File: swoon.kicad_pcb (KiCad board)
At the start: 2 copper layers, 109 x 86.9 mm, 130 parts, among them J1 3305-0-15-80-47-27-10-0, J10 3305-0-15-80-47-27-10-0, J11 3305-0-15-80-47-27-10-0, J12 3305-0-15-80-47-27-10-0, J13 3305-0-15-80-47-27-10-0, J14 3305-0-15-80-47-27-10-0, J15 3305-0-15-80-47-27-10-0, J16 3305-0-15-80-47-27-10-0, J17 3305-0-15-80-47-27-10-0, J18 3305-0-15-80-47-27-10-0, J19 3305-0-15-80-47-27-10-0, J2 3305-0-15-80-47-27-10-0, J20 3305-0-15-80-47-27-10-0, J21 3305-0-15-80-47-27-10-0, J22 3305-0-15-80-47-27-10-0, J23 3305-0-15-80-47-27-10-0, J24 3305-0-15-80-47-27-10-0, J25 3305-0-15-80-47-27-10-0, J26 3305-0-15-80-47-27-10-0, J27 3305-0-15-80-47-27-10-0, J28 3305-0-15-80-47-27-10-0, J29 3305-0-15-80-47-27-10-0, J3 3305-0-15-80-47-27-10-0, J30 3305-0-15-80-47-27-10-0, J31 3305-0-15-80-47-27-10-0, J32 3305-0-15-80-47-27-10-0, J33 3305-0-15-80-47-27-10-0, J34 3305-0-15-80-47-27-10-0, J35 3305-0-15-80-47-27-10-0, J36 3305-0-15-80-47-27-10-0, J37 3305-0-15-80-47-27-10-0, J38 3305-0-15-80-47-27-10-0, J39 3305-0-15-80-47-27-10-0, J4 3305-0-15-80-47-27-10-0, J40 3305-0-15-80-47-27-10-0, J41 3305-0-15-80-47-27-10-0, J42 3305-0-15-80-47-27-10-0, J43 3305-0-15-80-47-27-10-0, J44 3305-0-15-80-47-27-10-0, J45 3305-0-15-80-47-27-10-0, J46 3305-0-15-80-47-27-10-0, J47 3305-0-15-80-47-27-10-0, J48 3305-0-15-80-47-27-10-0, J49 3305-0-15-80-47-27-10-0, J5 3305-0-15-80-47-27-10-0, J50 3305-0-15-80-47-27-10-0, J51 3305-0-15-80-47-27-10-0, J52 3305-0-15-80-47-27-10-0, J53 3305-0-15-80-47-27-10-0, J54 3305-0-15-80-47-27-10-0, J55 3305-0-15-80-47-27-10-0, J56 3305-0-15-80-47-27-10-0, J57 3305-0-15-80-47-27-10-0, J58 3305-0-15-80-47-27-10-0, J59 3305-0-15-80-47-27-10-0, J6 3305-0-15-80-47-27-10-0, J60 3305-0-15-80-47-27-10-0, J61 3305-0-15-80-47-27-10-0, J62 3305-0-15-80-47-27-10-0, J63 3305-0-15-80-47-27-10-0, J64 3305-0-15-80-47-27-10-0, J65 3305-0-15-80-47-27-10-0, J66 3305-0-15-80-47-27-10-0, J67 3305-0-15-80-47-27-10-0, J68 3305-0-15-80-47-27-10-0, J69 MF254V-11-07-0743, J7 3305-0-15-80-47-27-10-0, J70 MF254V-11-07-0743, J71 MF254V-11-07-0743, J72 MF254V-11-07-0743, J73 Mill Max 0906-2-15-20-75-14-1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, J74 Mill Max 0906-2-15-20-75-14-1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, J75 JST SM02B-SRSS-TB(LF)(SN), J76 JST SM02B-SRSS-TB(LF)(SN), J8 3305-0-15-80-47-27-10-0, J9 3305-0-15-80-47-27-10-0, SW1 SW_Push, SW10 SW_Push, SW11 SW_Push, SW12 SW_Push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

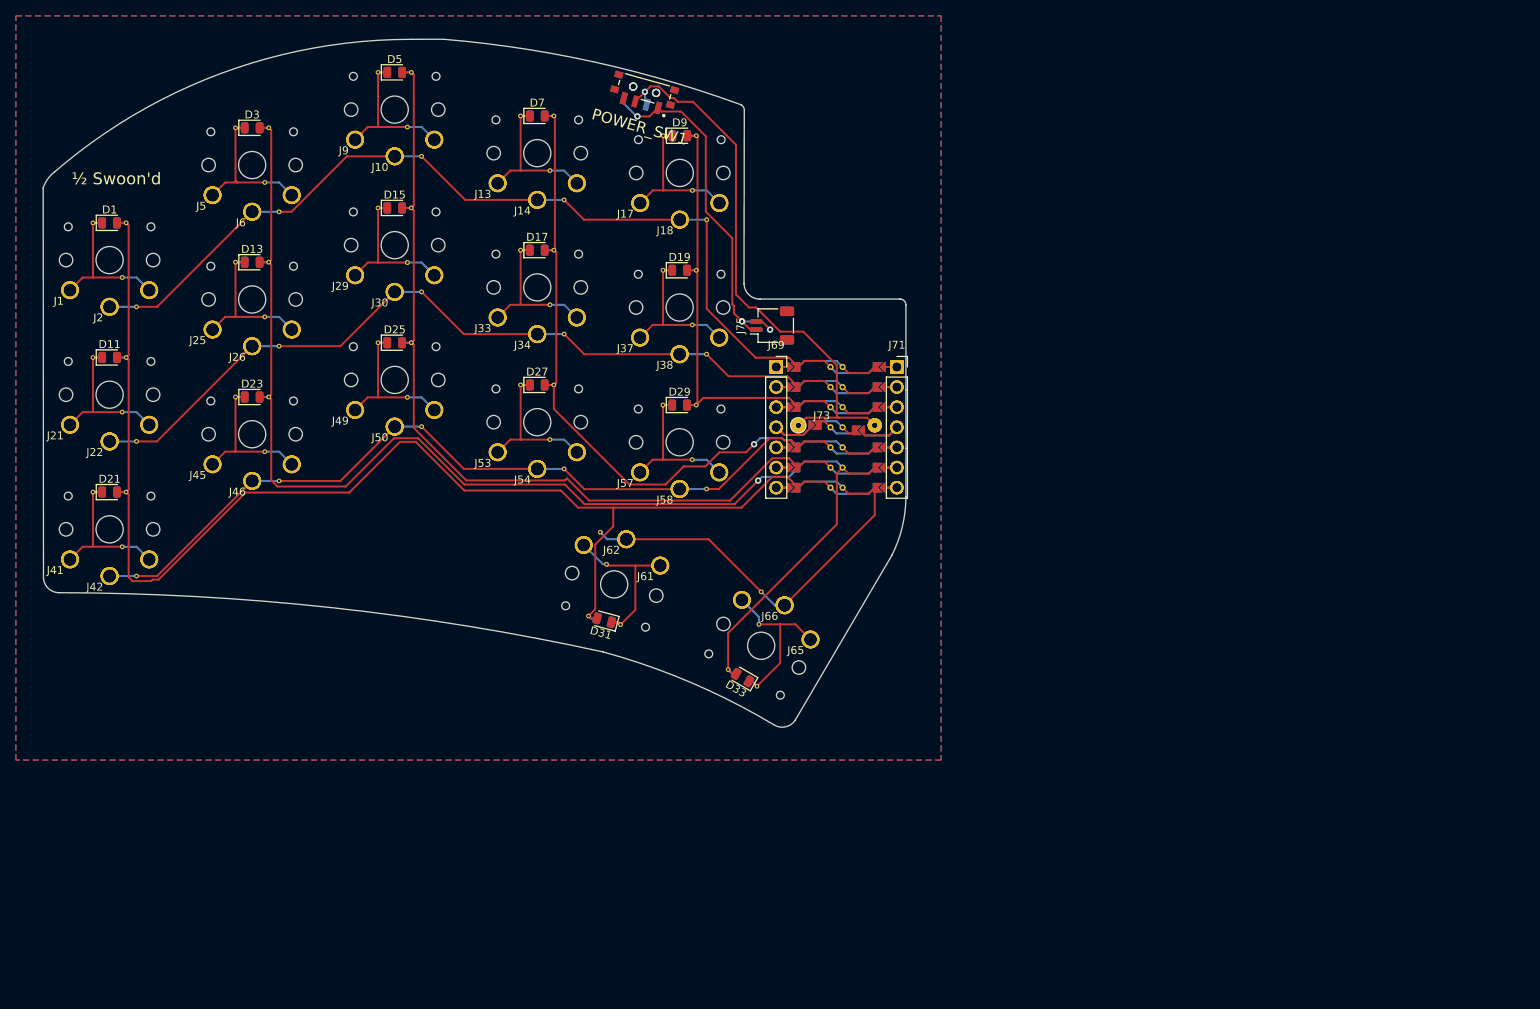
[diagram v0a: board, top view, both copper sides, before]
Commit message: position battery terminal & power switch
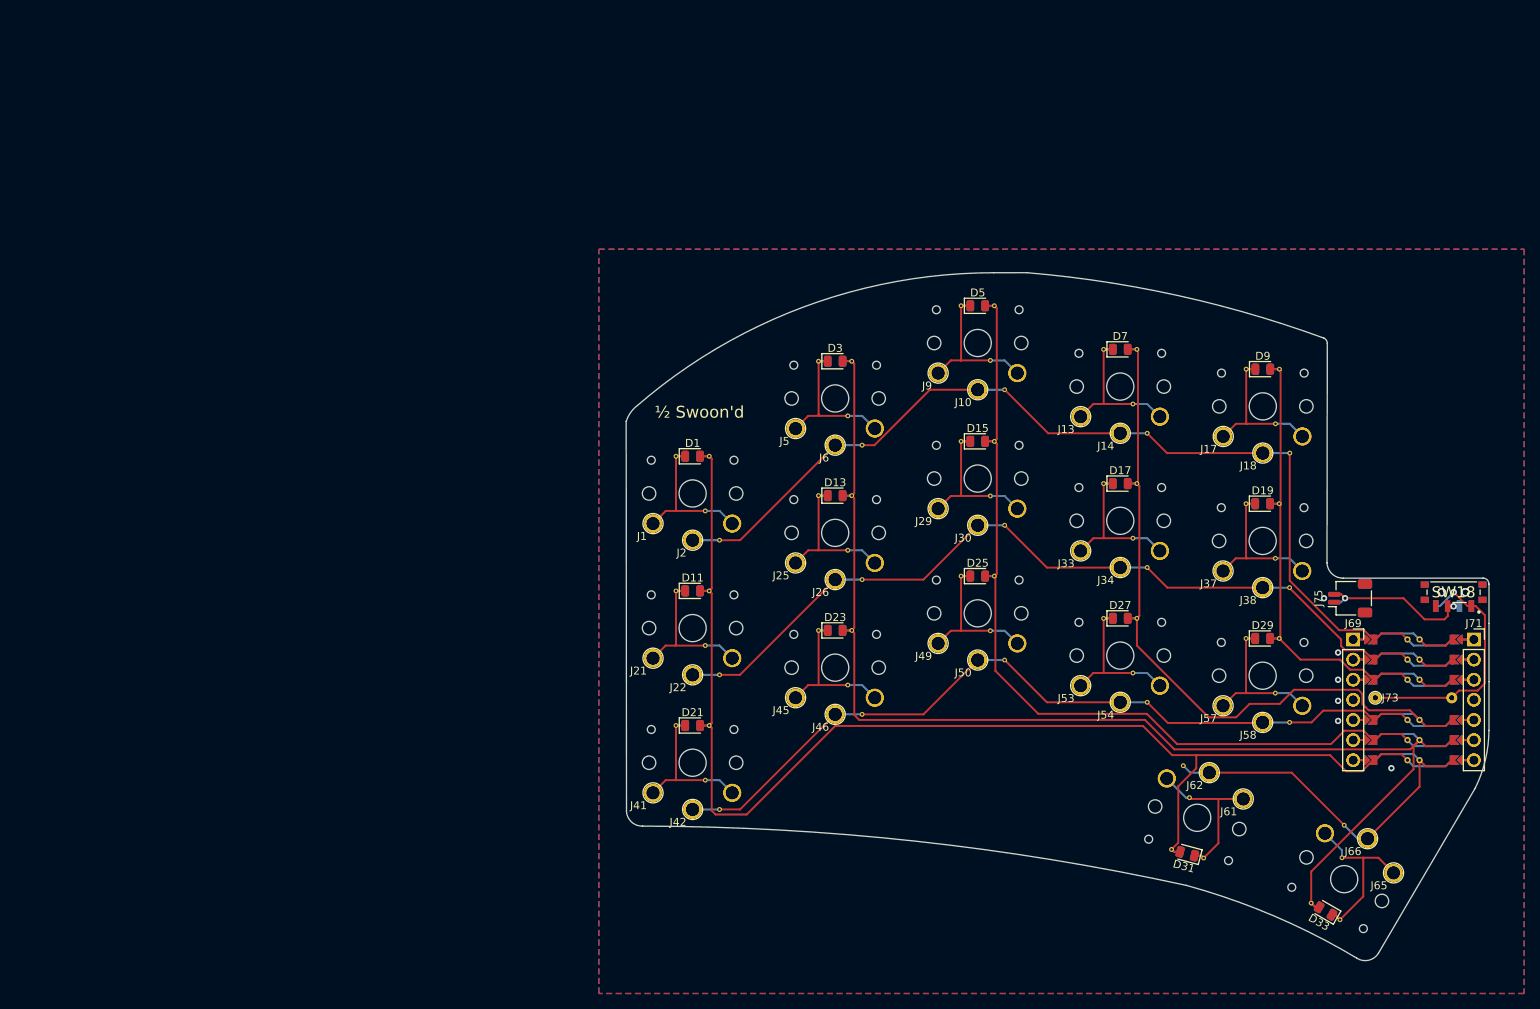
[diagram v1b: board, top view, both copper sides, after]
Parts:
- moved SW18 120.2 mm to (196.8, 88.0), turned to 180 degrees
- moved SW19 120.2 mm to (196.8, 88.0), turned to 0 degrees
- moved J75 80.7 mm to (183.7, 88.8)
- moved J76 80.7 mm to (183.7, 88.8)
- moved J74 80.6 mm to (196.6, 101.4)
- moved J69 80.6 mm to (184.1, 101.6), turned to -90 degrees
- moved J70 80.6 mm to (184.1, 101.6), turned to -90 degrees
- moved U1 80.6 mm to (191.7, 101.6)
- moved J71 80.6 mm to (199.3, 101.6), turned to -90 degrees
- moved J72 80.6 mm to (199.3, 101.6), turned to -90 degrees
- moved J73 80.6 mm to (186.9, 101.4)
- moved D31 79.3 mm to (163.2, 121.0)
- moved D32 79.3 mm to (163.2, 121.0)
- moved J10 79.3 mm to (136.7, 62.5)
- moved J12 79.3 mm to (136.7, 62.5)
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- renumbered POWER_SW1 to SW18, POWER_SW2 to SW19
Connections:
- J75 pad 1: Net-(J75-Pin_1) -> GND
- J75 pad 2: GND -> Net-(J75-Pin_2)
- J76 pad 1: Net-(J75-Pin_1) -> GND
- J76 pad 2: GND -> Net-(J75-Pin_2)
- SW18 pad 1: Net-(J75-Pin_1) -> /BAT+
- SW18 pad 2: /BAT+ -> Net-(J75-Pin_2)
- SW19 pad 1: Net-(J75-Pin_1) -> /BAT+
- SW19 pad 2: /BAT+ -> Net-(J75-Pin_2)
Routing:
- net Net-(J75-Pin_1): track 42.9 -> 0.00 mm, vias 2 -> 0
- net /BAT+: track 70.8 -> 31.3 mm
- net Net-(J75-Pin_2): track 0.00 -> 20.1 mm, vias 0 -> 2
- net /col1: track 167.4 -> 159.6 mm
- net /row4: track 46.7 -> 39.7 mm
- net /col2: track 160.8 -> 154.6 mm, vias 1 -> 0
- net /col4: track 82.1 -> 87.9 mm, vias 1 -> 0
- net /row1: track 112.4 -> 116.6 mm
- net /row3: track 101.2 -> 98.4 mm
- net GND: track 2.16 -> 0.00 mm, vias 1 -> 6
- net /row2: track 99.8 -> 101.6 mm
- net /col3: track 107.8 -> 106.6 mm
- net /col5: track 55.0 -> 55.5 mm
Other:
- outline, holes or cut-outs redrawn
